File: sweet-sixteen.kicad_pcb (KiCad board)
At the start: 2 copper layers, 113 x 105.4 mm, 87 parts, among them P1 SDA_I, P10 VIN_O, P11 GND_O, P12 SDA_O, P13 CLK_O, P14 LE_O, P15 ~OE_O, P2 CLK_I, P3 LE_I, P4 ~OE_I, P5 CONN_02X20, P6 5V_I, P7 VIN_I, P8 GND_I, P9 5V_O, U1 OKI-T/3-W40, U10 STP16CPC26, U11 STP16CPC26, U12 STP16CPC26, U13 74HCT08, U2 STP16CPC26, U3 OKI-T/3-W40, U4 STP16CPC26, U5 74HCT08, U6 STP16CPC26, U7 STP16CPC26, U8 STP16CPC26, U9 STP16CPC26

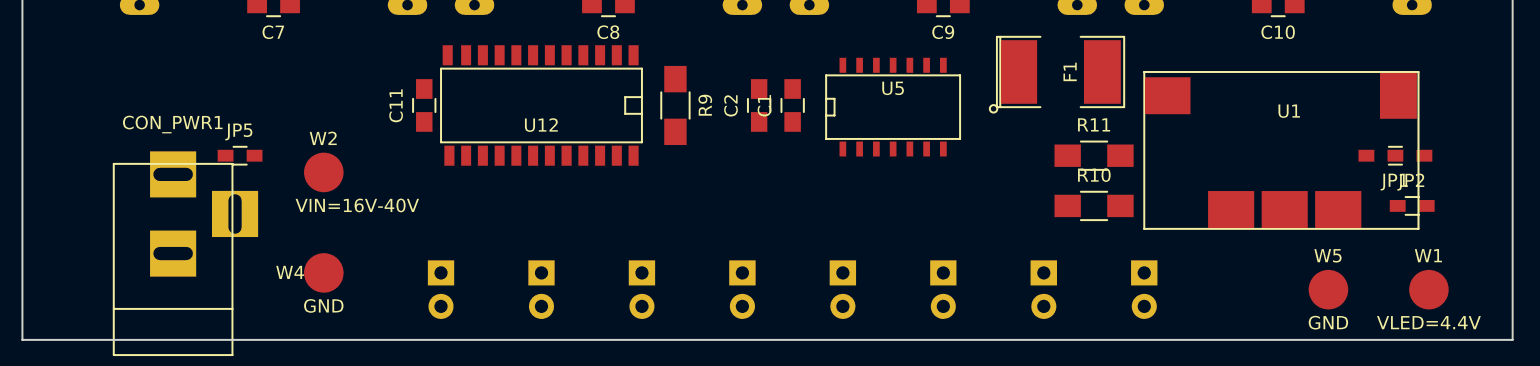
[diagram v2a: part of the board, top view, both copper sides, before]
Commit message: move labels
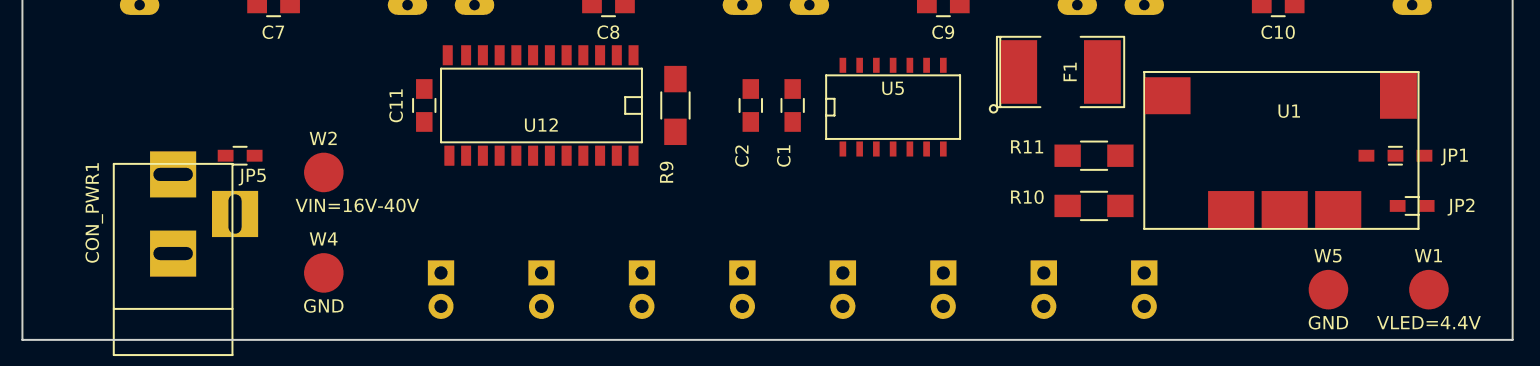
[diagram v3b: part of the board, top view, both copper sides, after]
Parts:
- JP1: value JUMPER3 -> (none)
- JP2, JP5: value JUMPER -> (none)
- moved C2 0.64 mm to (145.4, 119.4)
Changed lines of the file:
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@@
     (tags "capacitor 0805")
     (attr smd)
-    (fp_text reference C1 (at 0 -2.1 90) (layer F.SilkS)
-      (effects (font (size 1 1) (thickness 0.15)))
-    )
-    (fp_text value 10nf (at 0 2.1 90) (layer F.Fab)
+    (fp_text reference C1 (at -3.81 -0.635 90) (layer F.SilkS)
+      (effects (font (size 1 1) (thickness 0.15)))
+    )
+    (fp_text value 10nf (at -4.445 0.635 90) (layer F.Fab)
       (effects (font (size 1 1) (thickness 0.15)))
     )
@@
   )
   (module Capacitors_SMD:C_0805_HandSoldering (layer F.Cu)
-    (at 146.05 119.38 90)
+    (at 145.415 119.38 90)
     (descr "Capacitor SMD 0805, hand soldering")
     (tags "capacitor 0805")
     (attr smd)
-    (fp_text reference C2 (at 0 -2.1 90) (layer F.SilkS)
-      (effects (font (size 1 1) (thickness 0.15)))
-    )
-    (fp_text value 100nf (at 0 2.1 90) (layer F.Fab)
+    (fp_text reference C2 (at -3.81 -0.635 90) (layer F.SilkS)
+      (effects (font (size 1 1) (thickness 0.15)))
+    )
+    (fp_text value 100nf (at -5.08 0.635 90) (layer F.Fab)
       (effects (font (size 1 1) (thickness 0.15)))
     )
@@
     (descr "DC Barrel Jack")
     (tags "Power Jack")
-    (fp_text reference CON_PWR1 (at 10.09904 0 180) (layer F.SilkS)
-      (effects (font (size 1 1) (thickness 0.15)))
-    )
-    (fp_text value PWR (at 0 -5.99948 90) (layer F.Fab)
+    (fp_text reference CON_PWR1 (at 3.302 -6.096 270) (layer F.SilkS)
+      (effects (font (size 1 1) (thickness 0.15)))
+    )
+    (fp_text value PWR (at -3.302 -6.096 90) (layer F.Fab)
       (effects (font (size 1 1) (thickness 0.15)))
     )
@@
     (tags "resistor 1206")
     (attr smd)
-    (fp_text reference R9 (at 0 -2.3 270) (layer F.SilkS)
-      (effects (font (size 1 1) (thickness 0.15)))
-    )
-    (fp_text value 1k (at 0 2.3 270) (layer F.Fab)
+    (fp_text reference R9 (at 5.08 0.635 270) (layer F.SilkS)
+      (effects (font (size 1 1) (thickness 0.15)))
+    )
+    (fp_text value 1k (at 5.08 -0.635 270) (layer F.Fab)
       (effects (font (size 1 1) (thickness 0.15)))
     )
@@
     (tags "resistor 1206")
     (attr smd)
-    (fp_text reference R10 (at 0 -2.3) (layer F.SilkS)
-      (effects (font (size 1 1) (thickness 0.15)))
-    )
-    (fp_text value 1.2k (at 0 2.3) (layer F.Fab)
+    (fp_text reference R10 (at -5.08 -0.635) (layer F.SilkS)
+      (effects (font (size 1 1) (thickness 0.15)))
+    )
+    (fp_text value 1.2k (at -5.08 0.635) (layer F.Fab)
       (effects (font (size 1 1) (thickness 0.15)))
     )
@@
     (tags "resistor 1206")
     (attr smd)
-    (fp_text reference R11 (at 0 -2.3) (layer F.SilkS)
-      (effects (font (size 1 1) (thickness 0.15)))
-    )
-    (fp_text value 680 (at 0 2.3) (layer F.Fab)
+    (fp_text reference R11 (at -5.08 -0.635) (layer F.SilkS)
+      (effects (font (size 1 1) (thickness 0.15)))
+    )
+    (fp_text value 680 (at -5.08 0.635) (layer F.Fab)
       (effects (font (size 1 1) (thickness 0.15)))
     )
@@
     (descr "Mesurement Point, Round, SMD Pad, DM 3mm,")
     (tags "Mesurement Point, Round, SMD Pad, DM 3mm,")
-    (fp_text reference W4 (at -2.54 0) (layer F.SilkS)
+    (fp_text reference W4 (at 0 -2.54) (layer F.SilkS)
       (effects (font (size 1 1) (thickness 0.15)))
     )
@@
     (tags "resistor 0603")
     (attr smd)
-    (fp_text reference JP1 (at 0 -1.9 180) (layer F.SilkS)
-      (effects (font (size 1 1) (thickness 0.15)))
-    )
-    (fp_text value JUMPER3 (at 0 1.9 180) (layer F.Fab)
+    (fp_text reference JP1 (at -4.572 0 180) (layer F.SilkS)
+      (effects (font (size 1 1) (thickness 0.15)))
+    )
+    (fp_text value "" (at 0 -1.27 180) (layer F.Fab)
       (effects (font (size 1 1) (thickness 0.15)))
     )
@@
     (tags "resistor 0603")
     (attr smd)
-    (fp_text reference JP5 (at 0 -1.9) (layer F.SilkS)
-      (effects (font (size 1 1) (thickness 0.15)))
-    )
-    (fp_text value JUMPER (at 0 1.9) (layer F.Fab)
+    (fp_text reference JP5 (at 1.016 1.524) (layer F.SilkS)
+      (effects (font (size 1 1) (thickness 0.15)))
+    )
+    (fp_text value "" (at 0 1.9) (layer F.Fab)
       (effects (font (size 1 1) (thickness 0.15)))
     )
@@
     (tags "resistor 0603")
     (attr smd)
-    (fp_text reference JP2 (at 0 -1.9) (layer F.SilkS)
-      (effects (font (size 1 1) (thickness 0.15)))
-    )
-    (fp_text value JUMPER (at 0 1.9) (layer F.Fab)
-      (effects (font (size 1 1) (thickness 0.15)))
-    )
+    (fp_text reference JP2 (at 3.81 0) (layer F.SilkS)
+      (effects (font (size 1 1) (thickness 0.15)))
+    )
+    (fp_text value "" (at 3.81 1.905) (layer F.Fab)
+      (effects (font (size 1 1) (thickness 0.15)))
+    )

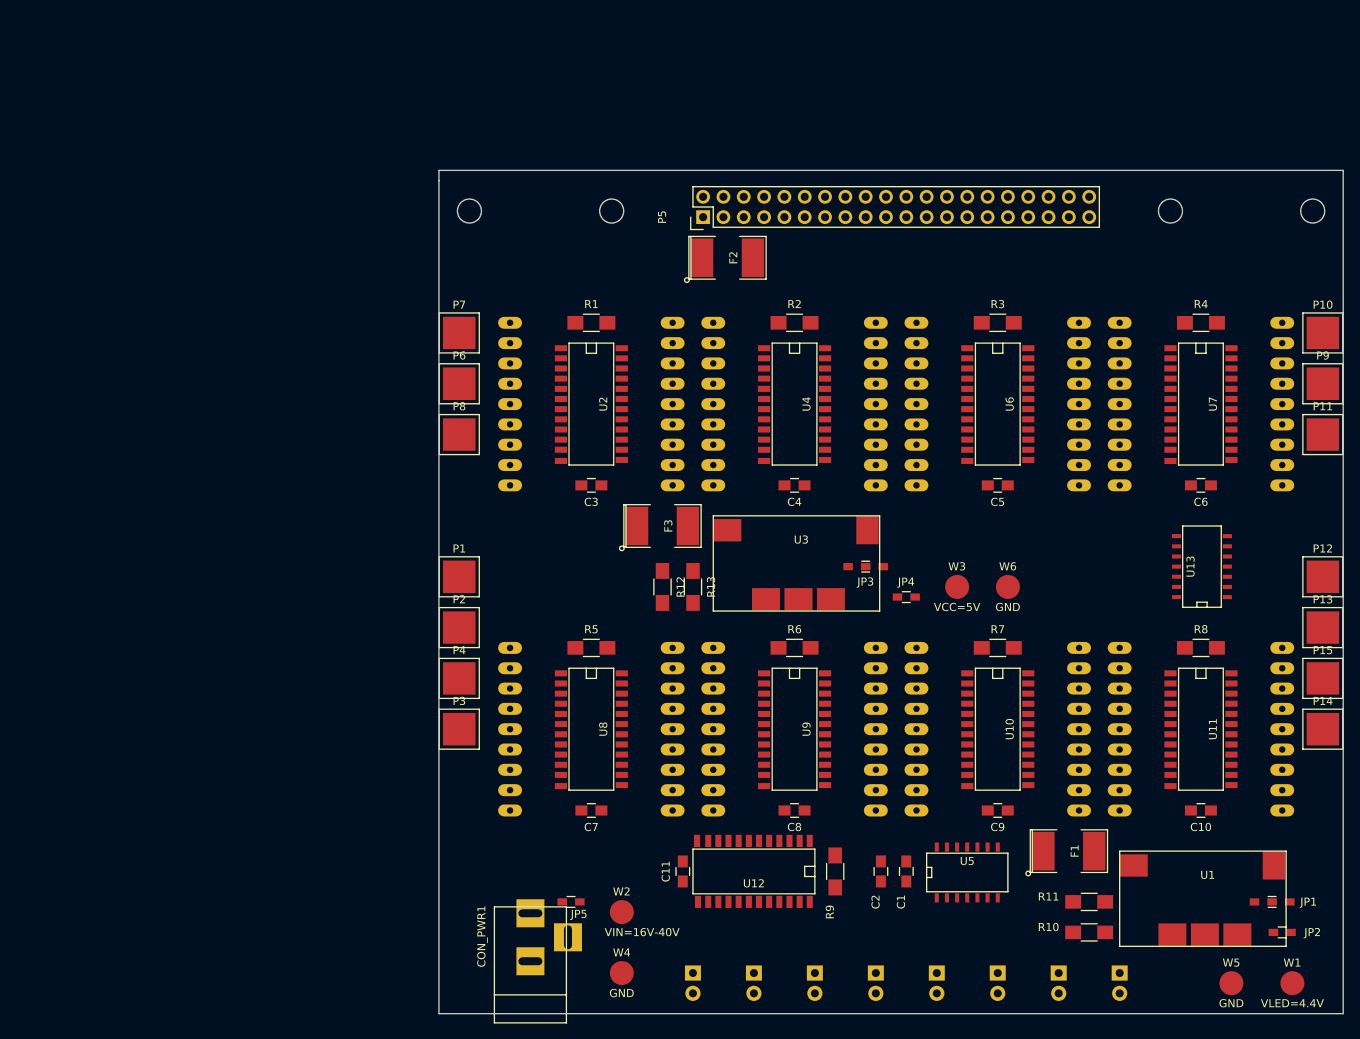
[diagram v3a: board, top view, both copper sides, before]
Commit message: redo pcb, footprints, pi interface
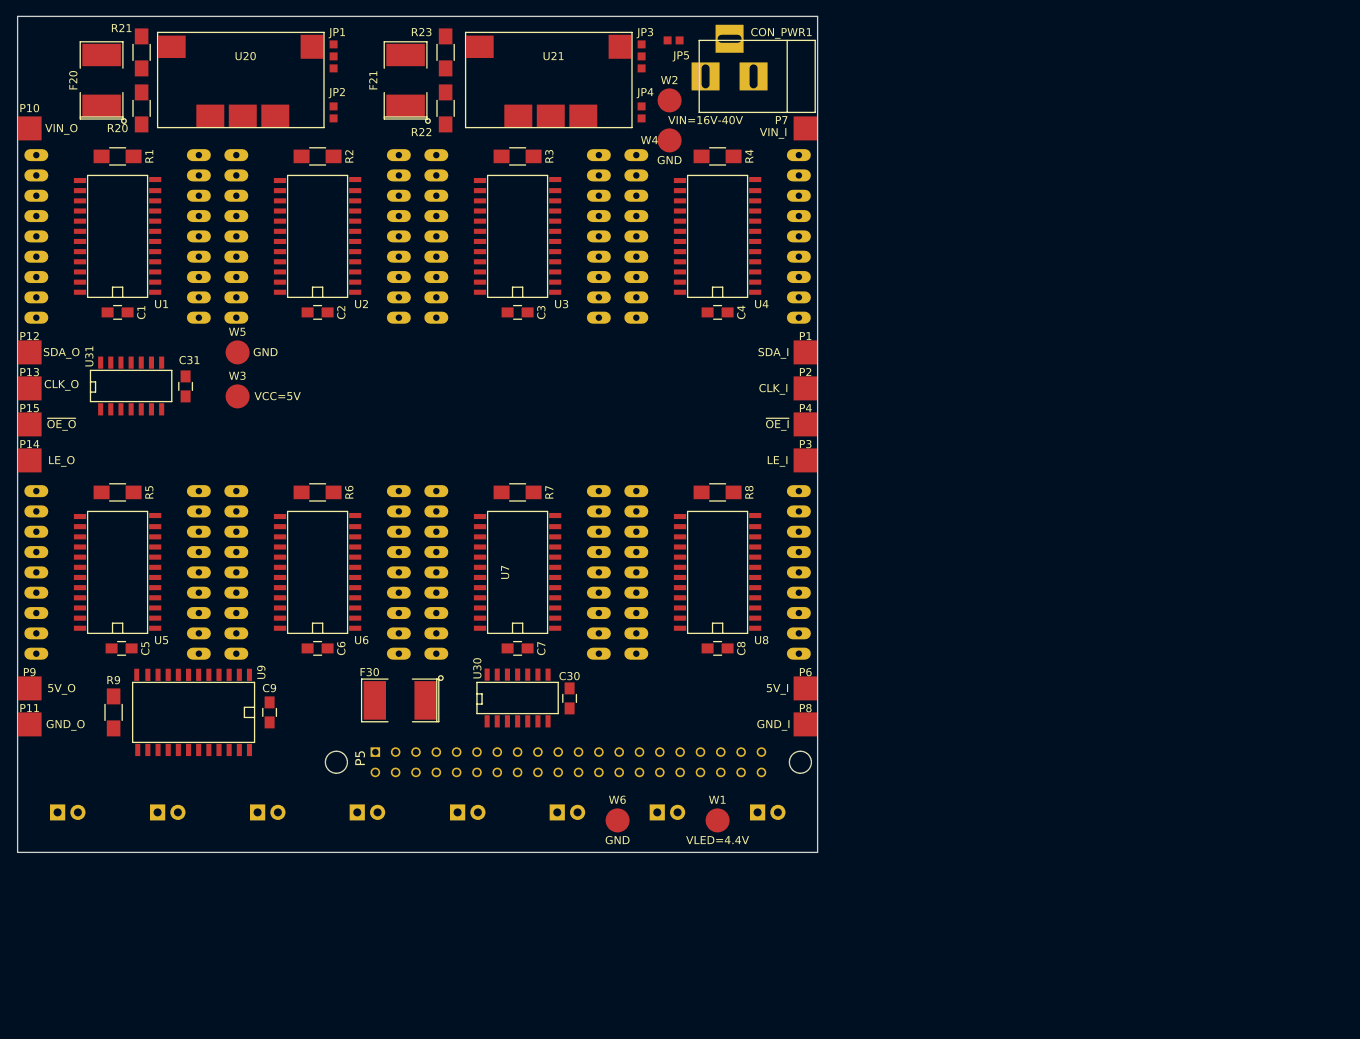
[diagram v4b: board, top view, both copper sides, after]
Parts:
- removed ? (x4): MountingHole_3mm, Mounting_Holes:MountingHole_3mm
- removed C10, C11: 10nf, Capacitors_SMD:C_0805_HandSoldering
- removed F1, F3: 1.2A F, SMD_Packages:SMD-2112_Pol
- removed F2: 2.5A S, SMD_Packages:SMD-2112_Pol
- removed R10, R12: 1.2k, Resistors_SMD:R_1206_HandSoldering
- removed R11: 680, Resistors_SMD:R_1206_HandSoldering
- removed R13: 270, Resistors_SMD:R_1206_HandSoldering
- removed U10, U11, U12: STP16CPC26, SMD_Packages:SOIC-24
- removed U13: 74HCT08, SMD_Packages:SOIC-14_N
- added C30: 10nf, Capacitors_SMD:C_0805_HandSoldering, F.Cu at (106.5, 97.8)
- added C31: 100nf, Capacitors_SMD:C_0805_HandSoldering, F.Cu at (58.5, 58.8)
- added F20: 1.2A F, SMD_Packages:SMD-2112_Pol, F.Cu at (48.0, 20.5)
- added F21: 1.2A F, SMD_Packages:SMD-2112_Pol, F.Cu at (86.0, 20.5)
- added F30: 2.5A S, SMD_Packages:SMD-2112_Pol, F.Cu at (85.3, 98.0)
- added R20: 1.2k, Resistors_SMD:R_1206_HandSoldering, F.Cu at (53.0, 24.0)
- added R21: 680, Resistors_SMD:R_1206_HandSoldering, F.Cu at (53.0, 17.0)
- added R22: 1.2k, Resistors_SMD:R_1206_HandSoldering, F.Cu at (91.0, 24.0)
- added R23: 270, Resistors_SMD:R_1206_HandSoldering, F.Cu at (91.0, 17.0)
- added U20: OKI-T/3-W40, oki-t3:OKI-T3, F.Cu at (55.0, 14.5)
- added U21: OKI-T/3-W40, oki-t3:OKI-T3, F.Cu at (93.5, 14.5)
- added U30: 74HCT08, chips:SN74HCT08D, F.Cu at (100.0, 97.7)
- added U31: 74HCT08, chips:SN74HCT08D, F.Cu at (51.7, 58.7)
- C2: value 100nf -> 10nf
- JP1: value (none) -> JUMPER3
- JP2, JP5: value (none) -> JUMPER
- P1, P10, P11, P12, P13, P14, P15, P2, P3, P4, P6, P7, P8, P9: footprint SMD_Packages:1Pin -> Measurement_Points:Measurement_Point_Square-SMD-Pad_Big
- P5: footprint Pin_Headers:Pin_Header_Straight_2x20 -> rpi-header:rpi-header
- U1, U3: value OKI-T/3-W40 -> STP16CPC26; footprint oki-t3:OKI-T3 -> chips:STP16CPC26MTR
- U2, U4, U6, U7, U8, U9: footprint SMD_Packages:SOIC-24 -> chips:STP16CPC26MTR
- U5: value 74HCT08 -> STP16CPC26; footprint SMD_Packages:SOIC-14_N -> chips:STP16CPC26MTR
- moved P9 166.1 mm to (39.0, 96.5)
- moved P11 165.7 mm to (39.0, 101.0)
- moved P14 165.1 mm to (39.0, 68.0)
- moved P15 164.7 mm to (39.0, 63.5)
- moved P13 164.4 mm to (39.0, 59.0)
- moved P12 164.1 mm to (39.0, 54.5)
- moved P10 163.7 mm to (39.0, 26.5)
- moved JP1 157.9 mm to (77.0, 17.5), turned to 270 degrees
- moved JP2 156.7 mm to (77.0, 24.5), turned to 270 degrees
- moved W5 147.1 mm to (65.0, 54.5)
- moved U1 147.0 mm to (50.0, 40.0), turned to 90 degrees
- moved C1 120.8 mm to (50.0, 49.5), turned to 0 degrees
- moved CON_PWR1 114.3 mm to (129.7, 20.0), turned to 180 degrees
- moved U5 112.6 mm to (50.0, 82.0), turned to 90 degrees
- moved C6 112.3 mm to (75.0, 91.5), turned to 0 degrees
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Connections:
- U1 pad 1: Net-(JP1-Pad2) -> GND
- U1 pad 2: Net-(F1-Pad2) -> /SDA
- U1 pad 3: GND -> /CLK
- U1 pad 4: Net-(R10-Pad2) -> /LE
- U1 pad 5: Net-(JP2-Pad1) -> Net-(AFF1-Pad8)
- U2 pad 10: Net-(AFF1-Pad9) -> Net-(AFF2-Pad3)
- U2 pad 11: Net-(AFF1-Pad8) -> Net-(AFF2-Pad2)
- U2 pad 12: Net-(AFF1-Pad4) -> Net-(AFF2-Pad1)
- U2 pad 13: Net-(AFF1-Pad3) -> Net-(AFF2-Pad18)
- U2 pad 14: Net-(AFF1-Pad2) -> Net-(AFF2-Pad17)
- U2 pad 15: Net-(AFF1-Pad17) -> Net-(AFF2-Pad16)
- U2 pad 16: Net-(AFF1-Pad15) -> Net-(AFF2-Pad15)
- U2 pad 17: Net-(AFF1-Pad6) -> Net-(AFF2-Pad14)
- U2 pad 18: Net-(AFF1-Pad14) -> Net-(AFF2-Pad13)
- U2 pad 19: Net-(AFF1-Pad7) -> Net-(AFF2-Pad9)
- U2 pad 2: /SDA -> Net-(U1-Pad22)
- U2 pad 20: Net-(AFF1-Pad5) -> Net-(AFF2-Pad10)
- U2 pad 23: Net-(R1-Pad2) -> Net-(R2-Pad2)
- U2 pad 5: Net-(AFF1-Pad1) -> Net-(AFF2-Pad8)
- U2 pad 6: Net-(AFF1-Pad18) -> Net-(AFF2-Pad7)
- U2 pad 7: Net-(AFF1-Pad16) -> Net-(AFF2-Pad6)
- U2 pad 8: Net-(AFF1-Pad13) -> Net-(AFF2-Pad5)
- U2 pad 9: Net-(AFF1-Pad10) -> Net-(AFF2-Pad4)
- U3 pad 1: Net-(JP3-Pad2) -> GND
- U3 pad 2: Net-(F3-Pad2) -> Net-(U2-Pad22)
- U3 pad 3: GND -> /CLK
- U3 pad 4: Net-(R12-Pad2) -> /LE
- U3 pad 5: Net-(JP4-Pad1) -> Net-(AFF3-Pad8)
- U4 pad 10: Net-(AFF2-Pad9) -> Net-(AFF4-Pad3)
- U4 pad 11: Net-(AFF2-Pad8) -> Net-(AFF4-Pad2)
- U4 pad 12: Net-(AFF2-Pad4) -> Net-(AFF4-Pad1)
- U4 pad 13: Net-(AFF2-Pad3) -> Net-(AFF4-Pad18)
- U4 pad 14: Net-(AFF2-Pad2) -> Net-(AFF4-Pad17)
- U4 pad 15: Net-(AFF2-Pad17) -> Net-(AFF4-Pad16)
- U4 pad 16: Net-(AFF2-Pad15) -> Net-(AFF4-Pad15)
- U4 pad 17: Net-(AFF2-Pad6) -> Net-(AFF4-Pad14)
- U4 pad 18: Net-(AFF2-Pad14) -> Net-(AFF4-Pad13)
- U4 pad 19: Net-(AFF2-Pad7) -> Net-(AFF4-Pad9)
- U4 pad 2: Net-(U2-Pad22) -> Net-(U3-Pad22)
- U4 pad 20: Net-(AFF2-Pad5) -> Net-(AFF4-Pad10)
- U4 pad 23: Net-(R2-Pad2) -> Net-(R4-Pad2)
- U4 pad 5: Net-(AFF2-Pad1) -> Net-(AFF4-Pad8)
- U4 pad 6: Net-(AFF2-Pad18) -> Net-(AFF4-Pad7)
- U4 pad 7: Net-(AFF2-Pad16) -> Net-(AFF4-Pad6)
- U4 pad 8: Net-(AFF2-Pad13) -> Net-(AFF4-Pad5)
- U4 pad 9: Net-(AFF2-Pad10) -> Net-(AFF4-Pad4)
- U5 pad 1: /~PI_OE -> GND
- U5 pad 10: /PI_SDA -> Net-(AFF5-Pad3)
- U5 pad 11: /LE -> Net-(AFF5-Pad2)
- U5 pad 12: /PI_LE -> Net-(AFF5-Pad1)
- U5 pad 13: /PI_LE -> Net-(AFF5-Pad18)
- U5 pad 14: VCC -> Net-(AFF5-Pad17)
- U5 pad 2: /~PI_OE -> Net-(U4-Pad22)
- U5 pad 3: /~OE -> /CLK
- U5 pad 4: /PI_CLK -> /LE
- U5 pad 5: /PI_CLK -> Net-(AFF5-Pad8)
- U5 pad 6: /CLK -> Net-(AFF5-Pad7)
- U5 pad 7: GND -> Net-(AFF5-Pad6)
- U5 pad 8: /SDA -> Net-(AFF5-Pad5)
- U5 pad 9: /PI_SDA -> Net-(AFF5-Pad4)
- U6 pad 10: Net-(AFF3-Pad9) -> Net-(AFF6-Pad3)
- U6 pad 11: Net-(AFF3-Pad8) -> Net-(AFF6-Pad2)
- U6 pad 12: Net-(AFF3-Pad4) -> Net-(AFF6-Pad1)
- U6 pad 13: Net-(AFF3-Pad3) -> Net-(AFF6-Pad18)
- U6 pad 14: Net-(AFF3-Pad2) -> Net-(AFF6-Pad17)
- U6 pad 15: Net-(AFF3-Pad17) -> Net-(AFF6-Pad16)
- U6 pad 16: Net-(AFF3-Pad15) -> Net-(AFF6-Pad15)
- U6 pad 17: Net-(AFF3-Pad6) -> Net-(AFF6-Pad14)
- U6 pad 18: Net-(AFF3-Pad14) -> Net-(AFF6-Pad13)
- U6 pad 19: Net-(AFF3-Pad7) -> Net-(AFF6-Pad9)
- U6 pad 2: Net-(U4-Pad22) -> Net-(U5-Pad22)
- U6 pad 20: Net-(AFF3-Pad5) -> Net-(AFF6-Pad10)
- U6 pad 23: Net-(R3-Pad2) -> Net-(R6-Pad2)
- U6 pad 5: Net-(AFF3-Pad1) -> Net-(AFF6-Pad8)
- U6 pad 6: Net-(AFF3-Pad18) -> Net-(AFF6-Pad7)
- U6 pad 7: Net-(AFF3-Pad16) -> Net-(AFF6-Pad6)
- U6 pad 8: Net-(AFF3-Pad13) -> Net-(AFF6-Pad5)
- U6 pad 9: Net-(AFF3-Pad10) -> Net-(AFF6-Pad4)
- U7 pad 10: Net-(AFF4-Pad9) -> Net-(AFF7-Pad3)
- U7 pad 11: Net-(AFF4-Pad8) -> Net-(AFF7-Pad2)
- U7 pad 12: Net-(AFF4-Pad4) -> Net-(AFF7-Pad1)
- U7 pad 13: Net-(AFF4-Pad3) -> Net-(AFF7-Pad18)
- U7 pad 14: Net-(AFF4-Pad2) -> Net-(AFF7-Pad17)
- U7 pad 15: Net-(AFF4-Pad17) -> Net-(AFF7-Pad16)
- U7 pad 16: Net-(AFF4-Pad15) -> Net-(AFF7-Pad15)
- U7 pad 17: Net-(AFF4-Pad6) -> Net-(AFF7-Pad14)
- U7 pad 18: Net-(AFF4-Pad14) -> Net-(AFF7-Pad13)
- U7 pad 19: Net-(AFF4-Pad7) -> Net-(AFF7-Pad9)
- U7 pad 20: Net-(AFF4-Pad5) -> Net-(AFF7-Pad10)
- U7 pad 23: Net-(R4-Pad2) -> Net-(R7-Pad2)
- U7 pad 5: Net-(AFF4-Pad1) -> Net-(AFF7-Pad8)
- U7 pad 6: Net-(AFF4-Pad18) -> Net-(AFF7-Pad7)
- U7 pad 7: Net-(AFF4-Pad16) -> Net-(AFF7-Pad6)
- U7 pad 8: Net-(AFF4-Pad13) -> Net-(AFF7-Pad5)
- U7 pad 9: Net-(AFF4-Pad10) -> Net-(AFF7-Pad4)
- U8 pad 10: Net-(AFF5-Pad9) -> Net-(AFF8-Pad3)
- U8 pad 11: Net-(AFF5-Pad8) -> Net-(AFF8-Pad2)
- U8 pad 12: Net-(AFF5-Pad4) -> Net-(AFF8-Pad1)
- U8 pad 13: Net-(AFF5-Pad3) -> Net-(AFF8-Pad18)
- U8 pad 14: Net-(AFF5-Pad2) -> Net-(AFF8-Pad17)
- U8 pad 15: Net-(AFF5-Pad17) -> Net-(AFF8-Pad16)
- U8 pad 16: Net-(AFF5-Pad15) -> Net-(AFF8-Pad15)
- U8 pad 17: Net-(AFF5-Pad6) -> Net-(AFF8-Pad14)
- U8 pad 18: Net-(AFF5-Pad14) -> Net-(AFF8-Pad13)
- U8 pad 19: Net-(AFF5-Pad7) -> Net-(AFF8-Pad9)
- U8 pad 20: Net-(AFF5-Pad5) -> Net-(AFF8-Pad10)
- U8 pad 23: Net-(R5-Pad2) -> Net-(R8-Pad2)
- U8 pad 5: Net-(AFF5-Pad1) -> Net-(AFF8-Pad8)
- U8 pad 6: Net-(AFF5-Pad18) -> Net-(AFF8-Pad7)
- U8 pad 7: Net-(AFF5-Pad16) -> Net-(AFF8-Pad6)
- U8 pad 8: Net-(AFF5-Pad13) -> Net-(AFF8-Pad5)
- U8 pad 9: Net-(AFF5-Pad10) -> Net-(AFF8-Pad4)
- U9 pad 10: Net-(AFF6-Pad9) -> Net-(AFF3-Pad12)
- U9 pad 11: Net-(AFF6-Pad8) -> Net-(AFF2-Pad12)
- U9 pad 12: Net-(AFF6-Pad4) -> Net-(AFF1-Pad12)
- U9 pad 13: Net-(AFF6-Pad3) -> Net-(D1-Pad1)
- U9 pad 14: Net-(AFF6-Pad2) -> Net-(D2-Pad1)
- U9 pad 15: Net-(AFF6-Pad17) -> Net-(D3-Pad1)
- U9 pad 16: Net-(AFF6-Pad15) -> Net-(D4-Pad1)
- U9 pad 17: Net-(AFF6-Pad6) -> Net-(D5-Pad1)
- U9 pad 18: Net-(AFF6-Pad14) -> Net-(D6-Pad1)
- U9 pad 19: Net-(AFF6-Pad7) -> Net-(D7-Pad1)
- U9 pad 20: Net-(AFF6-Pad5) -> Net-(D8-Pad1)
- U9 pad 23: Net-(R6-Pad2) -> Net-(R9-Pad2)
- U9 pad 5: Net-(AFF6-Pad1) -> Net-(AFF8-Pad12)
- U9 pad 6: Net-(AFF6-Pad18) -> Net-(AFF7-Pad12)
- U9 pad 7: Net-(AFF6-Pad16) -> Net-(AFF6-Pad12)
- U9 pad 8: Net-(AFF6-Pad13) -> Net-(AFF5-Pad12)
- U9 pad 9: Net-(AFF6-Pad10) -> Net-(AFF4-Pad12)
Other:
- board size 113 x 105.4 mm -> 100 x 104.5 mm
- rule pad_to_mask_clearance: 0.2 -> 0

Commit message: soldermask fixup
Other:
- rule pad_to_mask_clearance: 0 -> 0.254
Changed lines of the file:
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@@
     (39 F.Mask user)
     (40 Dwgs.User user)
-    (41 Cmts.User user)
-    (42 Eco1.User user)
-    (43 Eco2.User user)
-    (44 Edge.Cuts user)
-    (45 Margin user)
-    (46 B.CrtYd user)
-    (47 F.CrtYd user)
+    (41 Cmts.User user hide)
+    (42 Eco1.User user hide)
+    (43 Eco2.User user hide)
+    (44 Edge.Cuts user hide)
+    (45 Margin user hide)
+    (46 B.CrtYd user hide)
+    (47 F.CrtYd user hide)
     (48 B.Fab user)
     (49 F.Fab user)
@@
     (mod_text_size 1 1)
     (mod_text_width 0.15)
-    (pad_size 1.5 1.5)
-    (pad_drill 0.6)
-    (pad_to_mask_clearance 0)
+    (pad_size 2.8 3)
+    (pad_drill 0)
+    (pad_to_mask_clearance 0.254)
+    (solder_mask_min_width 0.1524)
     (aux_axis_origin 0 0)
     (visible_elements FFFFFF7F)
